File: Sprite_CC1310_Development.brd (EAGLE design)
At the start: 50 x 50 mm, 67 parts, among them U1 NCP1402

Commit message: still working
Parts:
- added U$1: HDMID, HDMID:HDMID
- moved C21 11.9 mm to (40.1, 23.6), flipped to the top, turned to 0 degrees
- moved COAX1 11.1 mm to (27.7, 5.09)
- moved R7 8.35 mm to (32.5, 17.1), turned to 270 degrees
- moved R20 7.33 mm to (29.7, 23.9), turned to 180 degrees
- moved LS1 6.65 mm to (33.7, 17.1), turned to 90 degrees
- moved C5 6.28 mm to (34.4, 11.0), turned to 270 degrees
- moved R15 5.91 mm to (27.7, 8.69)
- moved R16 5.91 mm to (30.4, 8.19)
- moved R22 5.91 mm to (22.4, 8.72)
- moved R17 5.89 mm to (25.1, 8.20)
- moved GPS 5.63 mm to (25.7, 14.9)
- moved R19 5.53 mm to (33.6, 20.7), turned to 270 degrees
- moved C20 5.49 mm to (37.7, 18.7), turned to 270 degrees
- moved R12 5.37 mm to (22.2, 22.2)
- moved R11 5.34 mm to (29.7, 22.8), turned to 180 degrees
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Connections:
- net GND: now also U$1.19, U$1.FOOT1, U$1.FOOT2, U$1.FOOT3, U$1.FOOT4
- net SWO: now also U$1.15, U$1.16
- net TDI: now also U$1.13, U$1.14
- net VDDS: now also U$1.17, U$1.18
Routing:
- net NAV: track 0.00 -> 35.5 mm, vias 0 -> 1
- net DCDC_SW: track 0.00 -> 20.0 mm
- net RXD: track 0.00 -> 18.0 mm, vias 0 -> 1
- net TDI: track 0.00 -> 17.8 mm
- net SWO: track 0.00 -> 17.7 mm
- net N$15: track 0.00 -> 15.6 mm
- net VDDR: track 7.53 -> 21.4 mm
- net TXD: track 0.00 -> 10.6 mm, vias 0 -> 1
- net SDA: track 7.86 -> 18.2 mm, vias 0 -> 2
- net N$6: track 17.3 -> 8.80 mm
- net SCL: track 7.02 -> 15.5 mm
- net N$14: track 0.00 -> 6.36 mm
- net VDDS: track 0.00 -> 6.28 mm, vias 0 -> 2
- net GND: track 0.00 -> 5.12 mm
- net ADC0: track 0.00 -> 4.84 mm, vias 0 -> 1
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
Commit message: still routing
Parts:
- moved C15 5.88 mm to (33.6, 8.17), turned to 0 degrees
- moved C16 5.79 mm to (25.6, 8.71), turned to 180 degrees
- moved R20 5.11 mm to (34.8, 23.8), turned to 270 degrees
- moved C14 5.04 mm to (33.7, 9.40), turned to 0 degrees
- moved C6 4.94 mm to (33.6, 11.8), turned to 0 degrees
- moved C17 4.90 mm to (22.4, 8.74)
- moved C13 4.73 mm to (33.6, 10.6), turned to 0 degrees
- moved C5 3.65 mm to (36.7, 8.16), turned to 180 degrees
- moved LS1 2.54 mm to (33.8, 14.5)
- moved R7 2.46 mm to (32.5, 14.7)
- moved C4 1.92 mm to (36.7, 9.40), turned to 180 degrees
- moved U$4 1.68 mm to (37.7, 23.5)
- moved C2 1.60 mm to (36.7, 11.8), turned to 180 degrees
- moved R19 1.08 mm to (33.9, 19.6), turned to 180 degrees
- moved L3 0.93 mm to (34.1, 23.3), turned to 0 degrees
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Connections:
- net GND: now also MICROCONTROLLER.32
- net JTAG_TCKC: now also U$1.5, U$1.6
- net JTAG_TMSC: now also U$1.3, U$1.4
- net RESET: now also U$1.13, U$1.14
- net RXD: now also U$1.17, U$1.18
- net SWO: now also U$1.11, U$1.12; no longer U$1.15, U$1.16
- net TDI: now also U$1.10, U$1.9; no longer U$1.13, U$1.14
- net TDO: now also U$1.7, U$1.8
- net TXD: now also U$1.15, U$1.16
- net VDDS: now also U$1.1, U$1.2; no longer U$1.17, U$1.18
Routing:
- net GND: track 5.12 -> 33.0 mm, vias 0 -> 3
- net VDDS: track 6.28 -> 23.8 mm, vias 2 -> 3
- net JTAG_TMSC: track 0.00 -> 17.4 mm
- net JTAG_TCKC: track 0.00 -> 16.7 mm
- net TDO: track 0.00 -> 16.7 mm
- net RESET: track 4.60 -> 16.0 mm, vias 0 -> 2
- net TXD: track 10.6 -> 19.8 mm, vias 1 -> 2
- net RXD: track 18.0 -> 25.8 mm, vias 1 -> 2
- net N$8: track 5.13 -> 9.55 mm
- net N$16: track 3.44 -> 1.46 mm
- net ADC0: track 4.84 -> 6.77 mm
- net N$19: track 1.43 -> 2.97 mm
- net SOLAR_CELLS: track 1.34 -> 0.00 mm
- net TDI: track 17.8 -> 16.6 mm
- net SWO: track 17.7 -> 16.7 mm
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
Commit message: closer
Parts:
- moved COAX 3.52 mm to (18.9, 23.3)
- moved R14 2.04 mm to (15.9, 23.0), turned to 270 degrees
- moved C26 1.95 mm to (23.8, 17.7), turned to 270 degrees
- moved C1 1.78 mm to (37.8, 17.1), turned to 0 degrees
- moved R8 1.76 mm to (34.1, 19.8)
- moved LS2 1.76 mm to (35.3, 20.0), turned to 270 degrees
- moved R13 1.43 mm to (16.3, 20.5)
- moved COAX1 1.38 mm to (27.7, 3.71)
- moved L1 1.25 mm to (31.5, 21.7)
- moved R21 1.08 mm to (21.5, 19.3)
- moved U$3 0.77 mm to (11.1, 11.6)
- moved L2 0.56 mm to (18.9, 19.7)
- moved C8 0.41 mm to (30.9, 23.7)
- moved R1 0.34 mm to (37.8, 16.0), turned to 180 degrees
- moved C5 0.33 mm to (36.7, 8.49)
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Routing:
- net COIL: track 0.00 -> 1211.6 mm, vias 0 -> 3
- net GND: track 33.0 -> 224.3 mm, vias 3 -> 14
- net VDDS: track 23.8 -> 127.5 mm, vias 3 -> 12
- net RXD: track 25.8 -> 49.7 mm
- net SOLAR_CELLS: track 0.00 -> 23.4 mm, vias 0 -> 1
- net TXD: track 19.8 -> 41.9 mm
- net DCDC_SW: track 20.9 -> 11.6 mm, vias 0 -> 2
- net N$21: track 4.10 -> 1.09 mm
- net N$16: track 1.46 -> 3.72 mm
- net N$20: track 0.00 -> 1.73 mm
- net N$14: track 6.36 -> 7.74 mm
- net N$26: track 6.42 -> 5.66 mm
- net N$10: track 3.83 -> 3.18 mm
- net VDDR: track 21.4 -> 20.9 mm, vias 0 -> 2
- net RESET: track 16.0 -> 16.3 mm, vias 2 -> 0
- added copper zone on layer 16, net GND
- added copper zone on layer 2, net GND
- added copper zone on layer 15, net VDDS

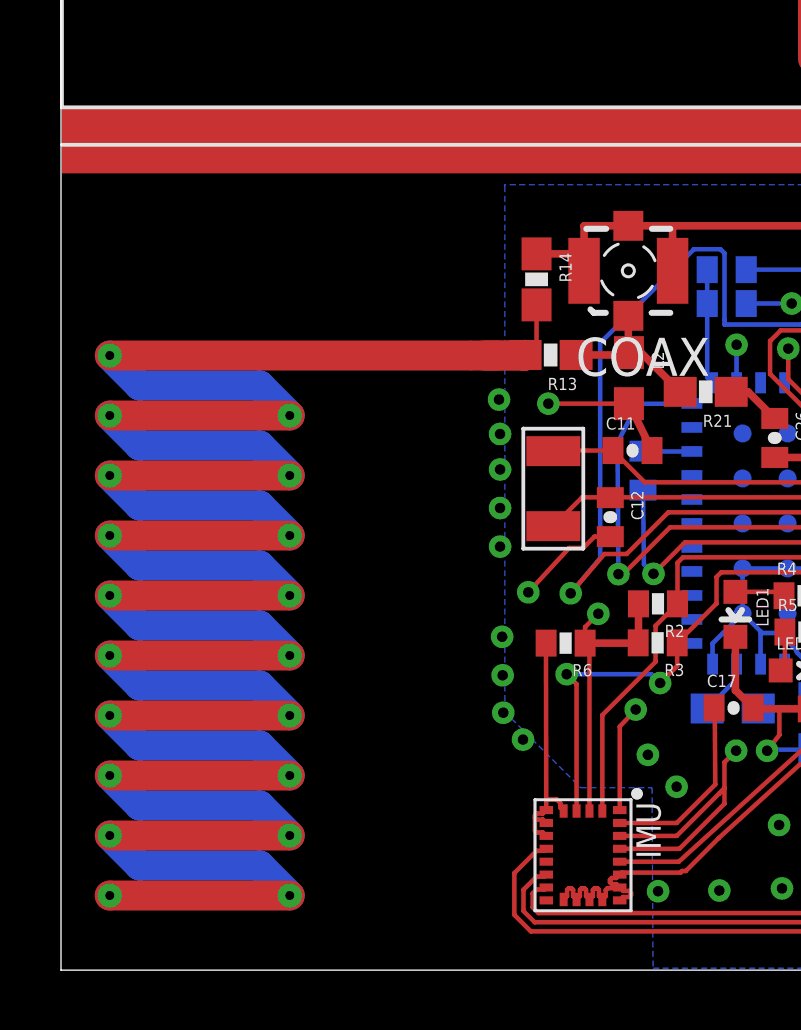
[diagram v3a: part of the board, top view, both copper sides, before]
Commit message: fixed antenna
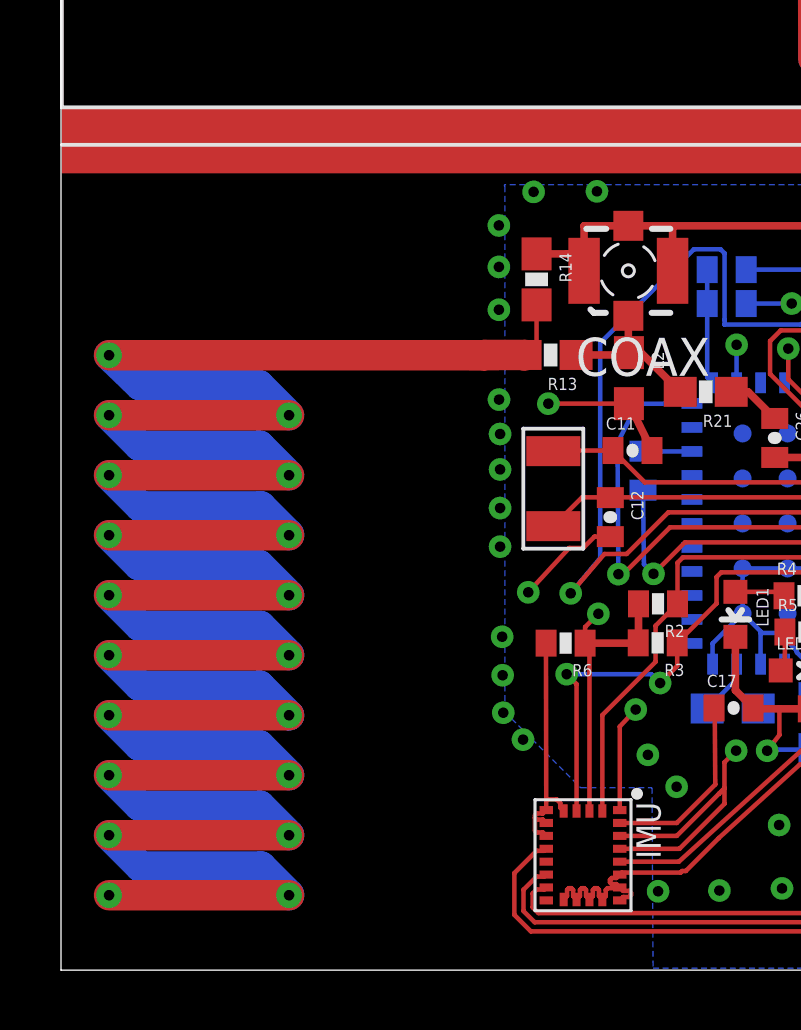
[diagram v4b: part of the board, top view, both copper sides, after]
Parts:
- removed U$3: 915_MHZ_PCB_ANTENNA, 915_MHZ_PCB_ANTENNA:915_MHZ_PCB_ANTENNA
- added U$6: PCB_ANTENNA, PCB_ANTENNA:PCB_ANTENNA
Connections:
- removed net N$10: R13.2, R14.2, U$3.ANTENNA
- new net ANTENNA: R13.2, R14.2, U$6.1, U$6.10, U$6.11, U$6.12, U$6.13, U$6.14, U$6.15, U$6.16, U$6.17, U$6.18, U$6.19, U$6.2, U$6.3, U$6.4, U$6.5, U$6.6, U$6.7, U$6.8, U$6.9, U$6.ANTENNA
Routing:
- net ANTENNA: track 0.00 -> 131.2 mm
- net N$10: track 3.18 -> 0.00 mm

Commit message: draft layout complete
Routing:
- net COIL: track 1211.6 -> 1352.2 mm
- net GND: track 224.3 -> 220.3 mm
- net SDA: track 17.4 -> 16.6 mm
